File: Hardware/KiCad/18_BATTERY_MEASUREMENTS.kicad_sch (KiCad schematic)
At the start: 0 parts

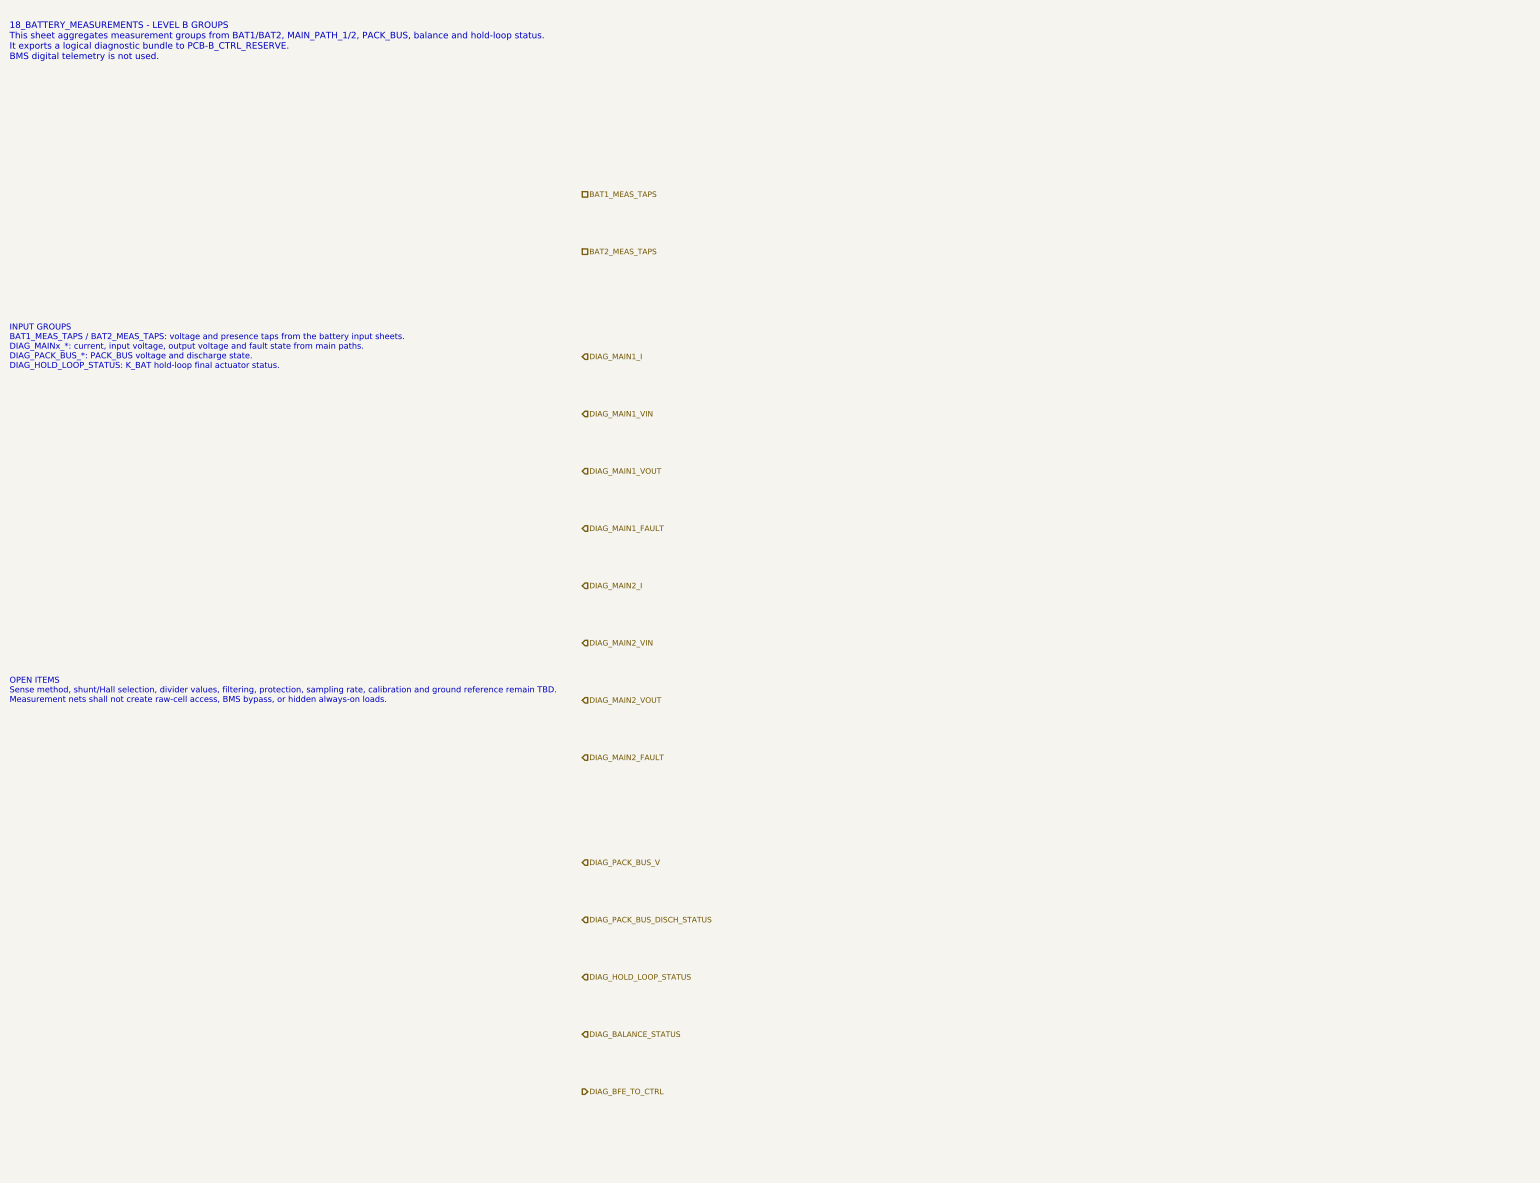
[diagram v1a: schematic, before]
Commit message: hardware: add remaining BFE symbol skeleton zones
Complete text-only symbol skeleton zones for remaining PCB-A BFE_POWER sheets.

Includes PACK_BUS, MAIN paths, measurements, deck balance, connectors and testpoints.
No real KiCad library symbols, part numbers, footprints, BOM entries or PCB layout are introduced.
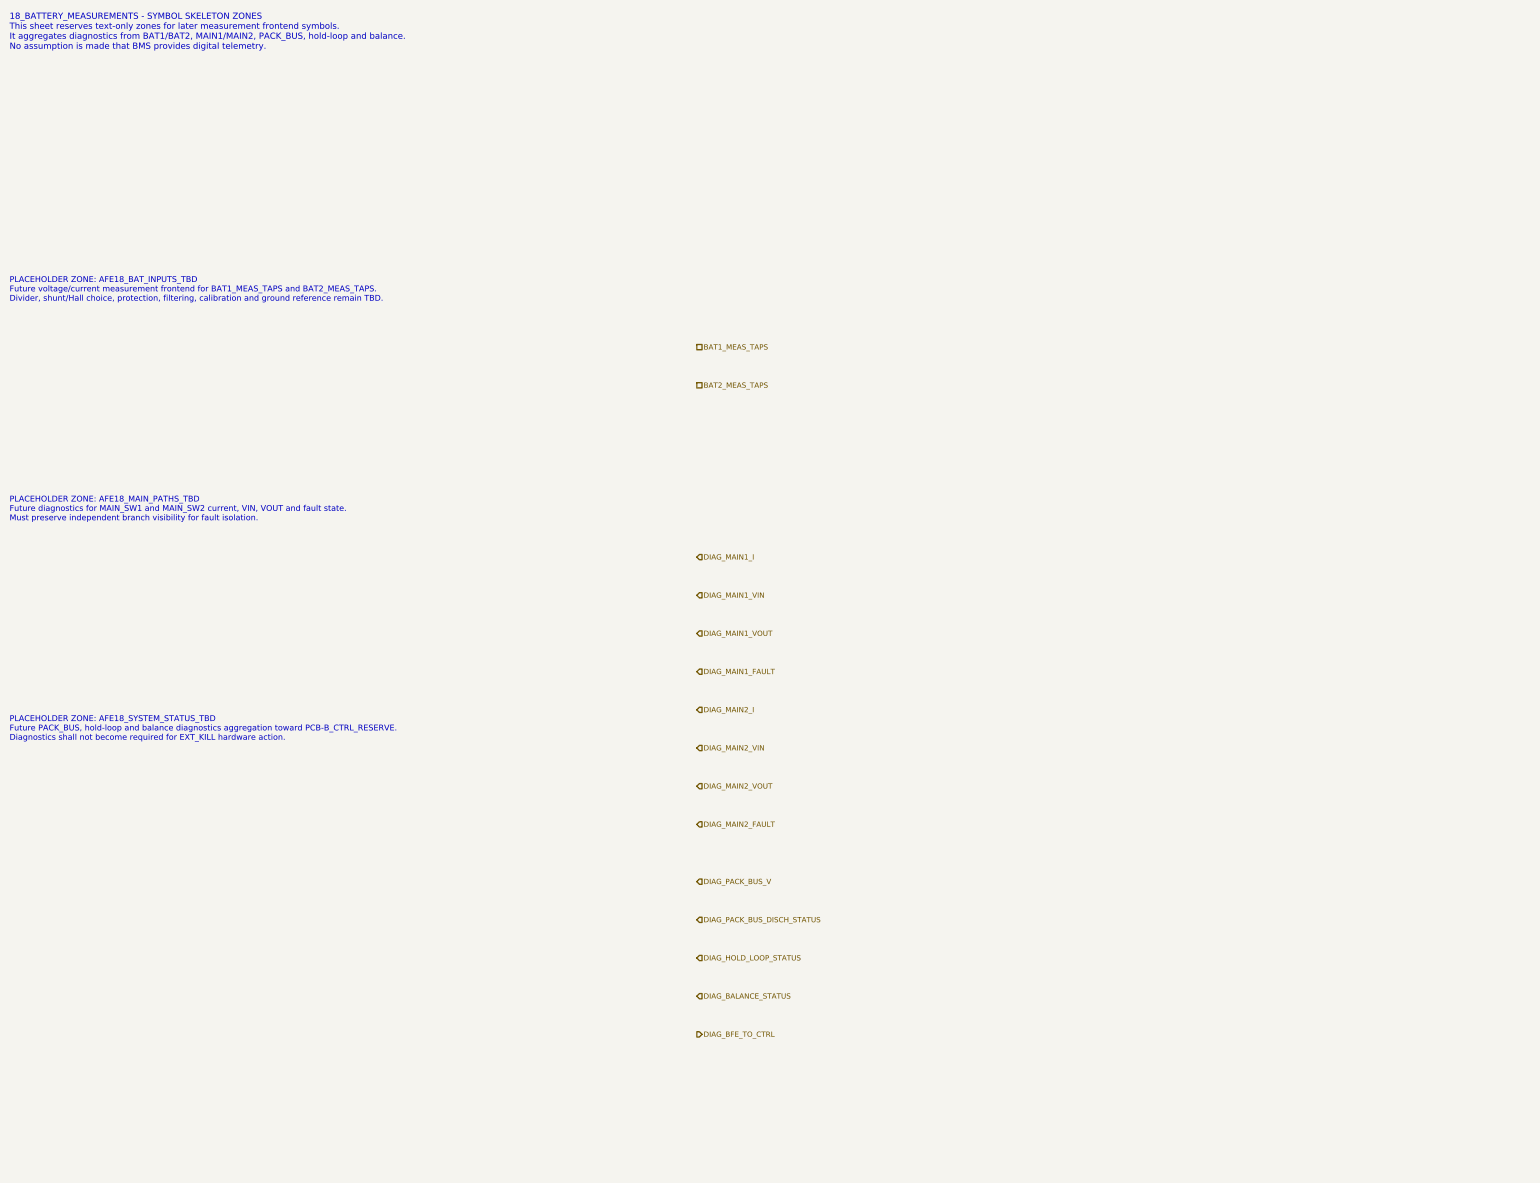
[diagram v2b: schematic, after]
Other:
- note added: "18_BATTERY_MEASUREMENTS - SYMBOL SKELETON ZONES This sheet reserves text-only zones for later measurement frontend symbols. It aggregates diagnostics from BAT1/BAT2, MAIN1/MAIN2, PACK_BUS, hold-loop and balance. No assumption is made that BMS provides digital telemetry."
- note added: "PLACEHOLDER ZONE: AFE18_BAT_INPUTS_TBD Future voltage/current measurement frontend for BAT1_MEAS_TAPS and BAT2_MEAS_TAPS. Divider, shunt/Hall choice, protection, filtering, calibration and ground reference remain TBD."
- note added: "PLACEHOLDER ZONE: AFE18_MAIN_PATHS_TBD Future diagnostics for MAIN_SW1 and MAIN_SW2 current, VIN, VOUT and fault state. Must preserve independent branch visibility for fault isolation."
- note added: "PLACEHOLDER ZONE: AFE18_SYSTEM_STATUS_TBD Future PACK_BUS, hold-loop and balance diagnostics aggregation toward PCB-B_CTRL_RESERVE. Diagnostics shall not become required for EXT_KILL hardware action."
- note removed: "18_BATTERY_MEASUREMENTS - LEVEL B GROUPS This sheet aggregates measurement groups from BAT1/BAT2, MAIN_PATH_1/2, PACK_BUS, balance and hold-loop status. It exports a logical diagnostic bundle to PCB-B_CTRL_RESERVE. BMS digital telemetry is not used."
- note removed: "INPUT GROUPS BAT1_MEAS_TAPS / BAT2_MEAS_TAPS: voltage and presence taps from the battery input sheets. DIAG_MAINx_*: current, input voltage, output voltage and fault state from main paths. DIAG_PACK_BUS_*: PACK_BUS voltage and discharge state. DIAG_HOLD_LOOP_STATUS: K_BAT hold-loop final actuator status."
- note removed: "OPEN ITEMS Sense method, shunt/Hall selection, divider values, filtering, protection, sampling rate, calibration and ground reference remain TBD. Measurement nets shall not create raw-cell access, BMS bypass, or hidden always-on loads."
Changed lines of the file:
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@@
 		(title "18_BATTERY_MEASUREMENTS - BFE sensing boundary")
 		(date "2026-07-15")
-		(rev "B1")
+		(rev "C1")
 		(company "Gonoboben/plataVM")
-		(comment 1 "Architecture Level B: measurement group names and diagnostic aggregation")
-		(comment 2 "No ADC frontend, current sensor, divider values or isolation topology selected")
+		(comment 1 "Symbol skeleton: BFE measurement AFE and diagnostic placeholders")
+		(comment 2 "No ADC frontend, isolation, sensor technology or part number selected")
 	)
-	(text "18_BATTERY_MEASUREMENTS - LEVEL B GROUPS\nThis sheet aggregates measurement groups from BAT1/BAT2, MAIN_PATH_1/2, PACK_BUS, balance and hold-loop status.\nIt exports a logical diagnostic bundle to PCB-B_CTRL_RESERVE.\nBMS digital telemetry is not used."
+	(text "18_BATTERY_MEASUREMENTS - SYMBOL SKELETON ZONES\nThis sheet reserves text-only zones for later measurement frontend symbols.\nIt aggregates diagnostics from BAT1/BAT2, MAIN1/MAIN2, PACK_BUS, hold-loop and balance.\nNo assumption is made that BMS provides digital telemetry."
 		(exclude_from_sim no)
-		(at 12 18 0)
-		(effects (font (size 1.35 1.35)) (justify left))
+		(at 12 16 0)
+		(effects (font (size 1.3 1.3)) (justify left))
 		(uuid "bfe-lb-00000018-0000-4000-8000-000000000101")
 	)
-	(text "INPUT GROUPS\nBAT1_MEAS_TAPS / BAT2_MEAS_TAPS: voltage and presence taps from the battery input sheets.\nDIAG_MAINx_*: current, input voltage, output voltage and fault state from main paths.\nDIAG_PACK_BUS_*: PACK_BUS voltage and discharge state.\nDIAG_HOLD_LOOP_STATUS: K_BAT hold-loop final actuator status."
+	(text "PLACEHOLDER ZONE: AFE18_BAT_INPUTS_TBD\nFuture voltage/current measurement frontend for BAT1_MEAS_TAPS and BAT2_MEAS_TAPS.\nDivider, shunt/Hall choice, protection, filtering, calibration and ground reference remain TBD."
 		(exclude_from_sim no)
-		(at 12 82 0)
-		(effects (font (size 1.25 1.25)) (justify left))
+		(at 12 70 0)
+		(effects (font (size 1.22 1.22)) (justify left))
 		(uuid "bfe-lb-00000018-0000-4000-8000-000000000102")
 	)
-	(text "OPEN ITEMS\nSense method, shunt/Hall selection, divider values, filtering, protection, sampling rate, calibration and ground reference remain TBD.\nMeasurement nets shall not create raw-cell access, BMS bypass, or hidden always-on loads."
+	(text "PLACEHOLDER ZONE: AFE18_MAIN_PATHS_TBD\nFuture diagnostics for MAIN_SW1 and MAIN_SW2 current, VIN, VOUT and fault state.\nMust preserve independent branch visibility for fault isolation."
 		(exclude_from_sim no)
-		(at 12 154 0)
-		(effects (font (size 1.25 1.25)) (justify left))
+		(at 12 116 0)
+		(effects (font (size 1.22 1.22)) (justify left))
 		(uuid "bfe-lb-00000018-0000-4000-8000-000000000103")
 	)
-	(hierarchical_label "BAT1_MEAS_TAPS" (shape passive) (exclude_from_sim no) (at 132 50 0) (effects (font (size 1.15 1.15)) (justify left)) (uuid "bfe-lb-00000018-0000-4000-8000-000000000201"))
-	(hierarchical_label "BAT2_MEAS_TAPS" (shape passive) (exclude_from_sim no) (at 132 62 0) (effects (font (size 1.15 1.15)) (justify left)) (uuid "bfe-lb-00000018-0000-4000-8000-000000000202"))
-	(hierarchical_label "DIAG_MAIN1_I" (shape input) (exclude_from_sim no) (at 132 84 0) (effects (font (size 1.15 1.15)) (justify left)) (uuid "bfe-lb-00000018-0000-4000-8000-000000000203"))
-	(hierarchical_label "DIAG_MAIN1_VIN" (shape input) (exclude_from_sim no) (at 132 96 0) (effects (font (size 1.15 1.15)) (justify left)) (uuid "bfe-lb-00000018-0000-4000-8000-000000000204"))
-	(hierarchical_label "DIAG_MAIN1_VOUT" (shape input) (exclude_from_sim no) (at 132 108 0) (effects (font (size 1.15 1.15)) (justify left)) (uuid "bfe-lb-00000018-0000-4000-8000-000000000205"))
-	(hierarchical_label "DIAG_MAIN1_FAULT" (shape input) (exclude_from_sim no) (at 132 120 0) (effects (font (size 1.15 1.15)) (justify left)) (uuid "bfe-lb-00000018-0000-4000-8000-000000000206"))
-	(hierarchical_label "DIAG_MAIN2_I" (shape input) (exclude_from_sim no) (at 132 132 0) (effects (font (size 1.15 1.15)) (justify left)) (uuid "bfe-lb-00000018-0000-4000-8000-000000000207"))
-	(hierarchical_label "DIAG_MAIN2_VIN" (shape input) (exclude_from_sim no) (at 132 144 0) (effects (font (size 1.15 1.15)) (justify left)) (uuid "bfe-lb-00000018-0000-4000-8000-000000000208"))
-	(hierarchical_label "DIAG_MAIN2_VOUT" (shape input) (exclude_from_sim no) (at 132 156 0) (effects (font (size 1.15 1.15)) (justify left)) (uuid "bfe-lb-00000018-0000-4000-8000-000000000209"))
-	(hierarchical_label "DIAG_MAIN2_FAULT" (shape input) (exclude_from_sim no) (at 132 168 0) (effects (font (size 1.15 1.15)) (justify left)) (uuid "bfe-lb-00000018-0000-4000-8000-000000000210"))
-	(hierarchical_label "DIAG_PACK_BUS_V" (shape input) (exclude_from_sim no) (at 132 190 0) (effects (font (size 1.15 1.15)) (justify left)) (uuid "bfe-lb-00000018-0000-4000-8000-000000000211"))
-	(hierarchical_label "DIAG_PACK_BUS_DISCH_STATUS" (shape input) (exclude_from_sim no) (at 132 202 0) (effects (font (size 1.15 1.15)) (justify left)) (uuid "bfe-lb-00000018-0000-4000-8000-000000000212"))
-	(hierarchical_label "DIAG_HOLD_LOOP_STATUS" (shape input) (exclude_from_sim no) (at 132 214 0) (effects (font (size 1.15 1.15)) (justify left)) (uuid "bfe-lb-00000018-0000-4000-8000-000000000213"))
-	(hierarchical_label "DIAG_BALANCE_STATUS" (shape input) (exclude_from_sim no) (at 132 226 0) (effects (font (size 1.15 1.15)) (justify left)) (uuid "bfe-lb-00000018-0000-4000-8000-000000000214"))
-	(hierarchical_label "DIAG_BFE_TO_CTRL" (shape output) (exclude_from_sim no) (at 132 238 0) (effects (font (size 1.15 1.15)) (justify left)) (uuid "bfe-lb-00000018-0000-4000-8000-000000000215"))
+	(text "PLACEHOLDER ZONE: AFE18_SYSTEM_STATUS_TBD\nFuture PACK_BUS, hold-loop and balance diagnostics aggregation toward PCB-B_CTRL_RESERVE.\nDiagnostics shall not become required for EXT_KILL hardware action."
+		(exclude_from_sim no)
+		(at 12 162 0)
+		(effects (font (size 1.22 1.22)) (justify left))
+		(uuid "bfe-lb-00000018-0000-4000-8000-000000000104")
+	)
+	(hierarchical_label "BAT1_MEAS_TAPS" (shape passive) (exclude_from_sim no) (at 156 82 0) (effects (font (size 1.1 1.1)) (justify left)) (uuid "bfe-lb-00000018-0000-4000-8000-000000000201"))
+	(hierarchical_label "BAT2_MEAS_TAPS" (shape passive) (exclude_from_sim no) (at 156 90 0) (effects (font (size 1.1 1.1)) (justify left)) (uuid "bfe-lb-00000018-0000-4000-8000-000000000202"))
+	(hierarchical_label "DIAG_MAIN1_I" (shape input) (exclude_from_sim no) (at 156 126 0) (effects (font (size 1.1 1.1)) (justify left)) (uuid "bfe-lb-00000018-0000-4000-8000-000000000203"))
+	(hierarchical_label "DIAG_MAIN1_VIN" (shape input) (exclude_from_sim no) (at 156 134 0) (effects (font (size 1.1 1.1)) (justify left)) (uuid "bfe-lb-00000018-0000-4000-8000-000000000204"))
+	(hierarchical_label "DIAG_MAIN1_VOUT" (shape input) (exclude_from_sim no) (at 156 142 0) (effects (font (size 1.1 1.1)) (justify left)) (uuid "bfe-lb-00000018-0000-4000-8000-000000000205"))
+	(hierarchical_label "DIAG_MAIN1_FAULT" (shape input) (exclude_from_sim no) (at 156 150 0) (effects (font (size 1.1 1.1)) (justify left)) (uuid "bfe-lb-00000018-0000-4000-8000-000000000206"))
+	(hierarchical_label "DIAG_MAIN2_I" (shape input) (exclude_from_sim no) (at 156 158 0) (effects (font (size 1.1 1.1)) (justify left)) (uuid "bfe-lb-00000018-0000-4000-8000-000000000207"))
+	(hierarchical_label "DIAG_MAIN2_VIN" (shape input) (exclude_from_sim no) (at 156 166 0) (effects (font (size 1.1 1.1)) (justify left)) (uuid "bfe-lb-00000018-0000-4000-8000-000000000208"))
+	(hierarchical_label "DIAG_MAIN2_VOUT" (shape input) (exclude_from_sim no) (at 156 174 0) (effects (font (size 1.1 1.1)) (justify left)) (uuid "bfe-lb-00000018-0000-4000-8000-000000000209"))
+	(hierarchical_label "DIAG_MAIN2_FAULT" (shape input) (exclude_from_sim no) (at 156 182 0) (effects (font (size 1.1 1.1)) (justify left)) (uuid "bfe-lb-00000018-0000-4000-8000-000000000210"))
+	(hierarchical_label "DIAG_PACK_BUS_V" (shape input) (exclude_from_sim no) (at 156 194 0) (effects (font (size 1.1 1.1)) (justify left)) (uuid "bfe-lb-00000018-0000-4000-8000-000000000211"))
+	(hierarchical_label "DIAG_PACK_BUS_DISCH_STATUS" (shape input) (exclude_from_sim no) (at 156 202 0) (effects (font (size 1.1 1.1)) (justify left)) (uuid "bfe-lb-00000018-0000-4000-8000-000000000212"))
+	(hierarchical_label "DIAG_HOLD_LOOP_STATUS" (shape input) (exclude_from_sim no) (at 156 210 0) (effects (font (size 1.1 1.1)) (justify left)) (uuid "bfe-lb-00000018-0000-4000-8000-000000000213"))
+	(hierarchical_label "DIAG_BALANCE_STATUS" (shape input) (exclude_from_sim no) (at 156 218 0) (effects (font (size 1.1 1.1)) (justify left)) (uuid "bfe-lb-00000018-0000-4000-8000-000000000214"))
+	(hierarchical_label "DIAG_BFE_TO_CTRL" (shape output) (exclude_from_sim no) (at 156 226 0) (effects (font (size 1.1 1.1)) (justify left)) (uuid "bfe-lb-00000018-0000-4000-8000-000000000215"))
 )
